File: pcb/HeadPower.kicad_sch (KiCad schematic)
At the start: 9 parts

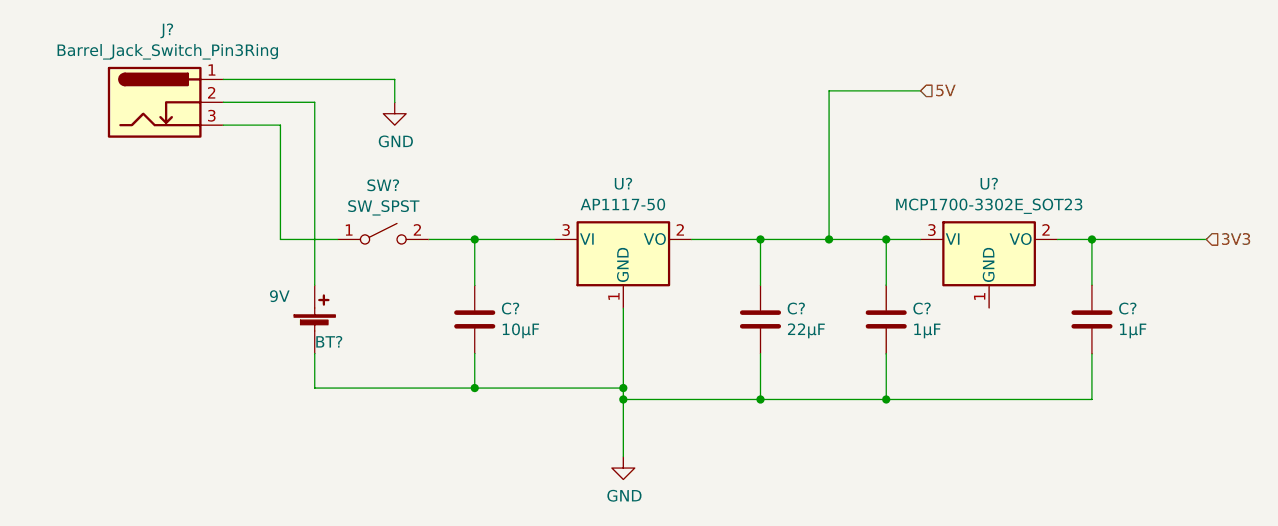
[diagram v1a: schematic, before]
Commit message: Adds line protection
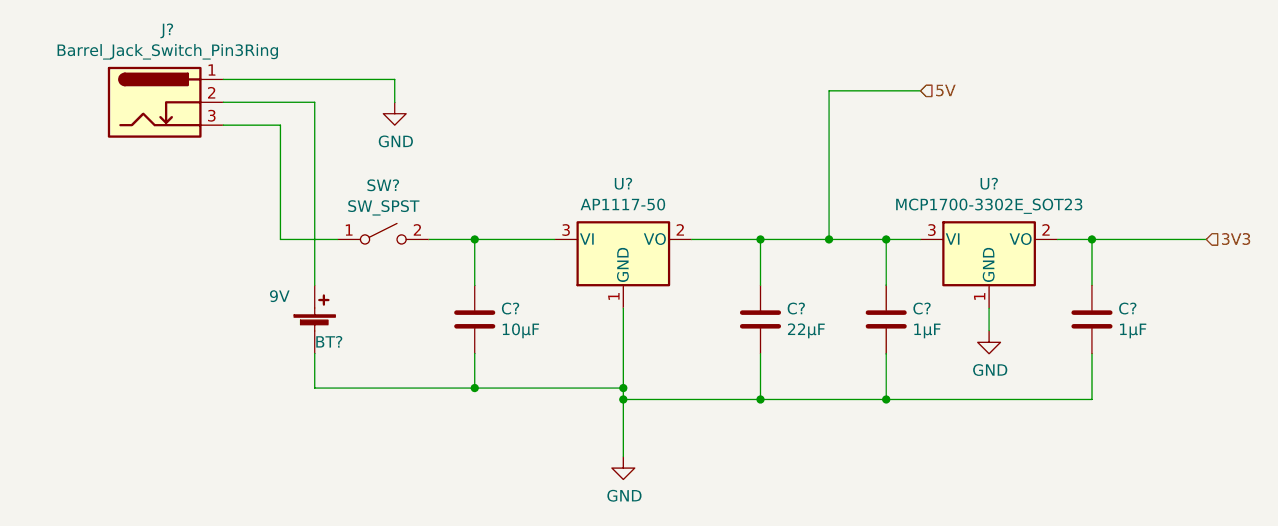
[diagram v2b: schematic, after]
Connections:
- net GND: now also U?.1 (GND)
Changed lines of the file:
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@@
+    (stroke (width 0) (type default) (color 0 0 0 0))
+  )
+  (wire (pts (xy 154.94 77.47) (xy 154.94 80.01))
     (stroke (width 0) (type default) (color 0 0 0 0))
   )
@@
     (pin "2")
   )
+  (symbol (lib_id "power:GND") (at 154.94 80.01 0) (unit 1)
+    (in_bom yes) (on_board yes)
+    (property "Reference" "#PWR?" (id 0) (at 154.94 86.36 0)
+      (effects (font (size 1.27 1.27)) hide)
+    )
+    (property "Value" "GND" (id 1) (at 155.067 84.4042 0))
+    (property "Footprint" "" (id 2) (at 154.94 80.01 0)
+      (effects (font (size 1.27 1.27)) hide)
+    )
+    (property "Datasheet" "" (id 3) (at 154.94 80.01 0)
+      (effects (font (size 1.27 1.27)) hide)
+    )
+    (pin "1")
+  )
 )

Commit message: Adds current control for the display adapter back light
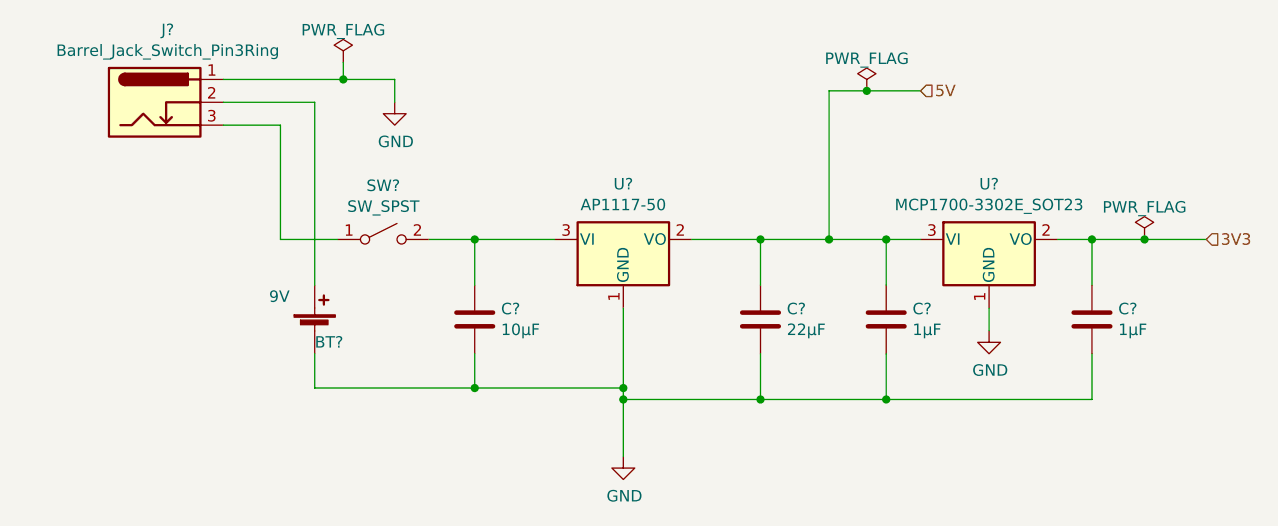
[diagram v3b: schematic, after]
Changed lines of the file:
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@@
   (junction (at 129.54 69.85) (diameter 0) (color 0 0 0 0)
   )
+  (junction (at 172.212 69.85) (diameter 0) (color 0 0 0 0)
+  )
   (junction (at 114.3 86.36) (diameter 0) (color 0 0 0 0)
   )
+  (junction (at 83.185 52.07) (diameter 0) (color 0 0 0 0)
+  )
   (junction (at 114.3 87.63) (diameter 0) (color 0 0 0 0)
   )
@@
   (junction (at 143.51 69.85) (diameter 0) (color 0 0 0 0)
   )
+  (junction (at 141.351 53.34) (diameter 0) (color 0 0 0 0)
+  )
   (wire (pts (xy 129.54 69.85) (xy 121.92 69.85))
     (stroke (width 0) (type default) (color 0 0 0 0))
@@
     (stroke (width 0) (type default) (color 0 0 0 0))
   )
-  (wire (pts (xy 166.37 69.85) (xy 179.07 69.85))
+  (wire (pts (xy 166.37 69.85) (xy 172.212 69.85))
     (stroke (width 0) (type default) (color 0 0 0 0))
   )
@@
     (stroke (width 0) (type default) (color 0 0 0 0))
   )
-  (wire (pts (xy 69.85 52.07) (xy 88.9 52.07))
-    (stroke (width 0) (type default) (color 0 0 0 0))
-  )
-  (wire (pts (xy 137.16 53.34) (xy 147.32 53.34))
+  (wire (pts (xy 69.85 52.07) (xy 83.185 52.07))
+    (stroke (width 0) (type default) (color 0 0 0 0))
+  )
+  (wire (pts (xy 137.16 53.34) (xy 141.351 53.34))
     (stroke (width 0) (type default) (color 0 0 0 0))
   )
@@
     (stroke (width 0) (type default) (color 0 0 0 0))
   )
+  (wire (pts (xy 141.351 53.34) (xy 147.32 53.34))
+    (stroke (width 0) (type default) (color 0 0 0 0))
+  )
   (wire (pts (xy 97.79 69.85) (xy 106.68 69.85))
     (stroke (width 0) (type default) (color 0 0 0 0))
@@
     (stroke (width 0) (type default) (color 0 0 0 0))
   )
+  (wire (pts (xy 83.185 50.165) (xy 83.185 52.07))
+    (stroke (width 0) (type default) (color 0 0 0 0))
+  )
+  (wire (pts (xy 172.212 69.85) (xy 179.07 69.85))
+    (stroke (width 0) (type default) (color 0 0 0 0))
+  )
   (wire (pts (xy 137.16 69.85) (xy 143.51 69.85))
     (stroke (width 0) (type default) (color 0 0 0 0))
@@
   )
   (wire (pts (xy 80.01 74.93) (xy 80.01 54.61))
+    (stroke (width 0) (type default) (color 0 0 0 0))
+  )
+  (wire (pts (xy 83.185 52.07) (xy 88.9 52.07))
     (stroke (width 0) (type default) (color 0 0 0 0))
   )
@@
     (pin "2")
   )
+  (symbol (lib_id "power:PWR_FLAG") (at 83.185 50.165 0) (unit 1)
+    (in_bom yes) (on_board yes) (fields_autoplaced)
+    (property "Reference" "#FLG?" (id 0) (at 83.185 48.26 0)
+      (effects (font (size 1.27 1.27)) hide)
+    )
+    (property "Value" "PWR_FLAG" (id 1) (at 83.185 46.5892 0))
+    (property "Footprint" "" (id 2) (at 83.185 50.165 0)
+      (effects (font (size 1.27 1.27)) hide)
+    )
+    (property "Datasheet" "~" (id 3) (at 83.185 50.165 0)
+      (effects (font (size 1.27 1.27)) hide)
+    )
+    (pin "1")
+  )
   (symbol (lib_id "power:GND") (at 154.94 80.01 0) (unit 1)
     (in_bom yes) (on_board yes)
@@
       (effects (font (size 1.27 1.27)) hide)
     )
+    (pin "1")
+  )
+  (symbol (lib_id "power:PWR_FLAG") (at 141.351 53.34 0) (unit 1)
+    (in_bom yes) (on_board yes) (fields_autoplaced)
+    (property "Reference" "#FLG?" (id 0) (at 141.351 51.435 0)
+      (effects (font (size 1.27 1.27)) hide)
+    )
+    (property "Value" "PWR_FLAG" (id 1) (at 141.351 49.7642 0))
+    (property "Footprint" "" (id 2) (at 141.351 53.34 0)
+      (effects (font (size 1.27 1.27)) hide)
+    )
+    (property "Datasheet" "~" (id 3) (at 141.351 53.34 0)
+      (effects (font (size 1.27 1.27)) hide)
+    )
+    (pin "1")
+  )
+  (symbol (lib_id "power:PWR_FLAG") (at 172.212 69.85 0) (unit 1)
+    (in_bom yes) (on_board yes) (fields_autoplaced)
+    (property "Reference" "#FLG?" (id 0) (at 172.212 67.945 0)
+      (effects (font (size 1.27 1.27)) hide)
+    )
+    (property "Value" "PWR_FLAG" (id 1) (at 172.212 66.2742 0))
+    (property "Footprint" "" (id 2) (at 172.212 69.85 0)
+      (effects (font (size 1.27 1.27)) hide)
+    )
+    (property "Datasheet" "~" (id 3) (at 172.212 69.85 0)
+      (effects (font (size 1.27 1.27)) hide)
+    )

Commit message: Schematic complete
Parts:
- gave numbers to parts that had none: 9
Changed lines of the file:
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@@
   (junction (at 129.54 69.85) (diameter 0) (color 0 0 0 0)
   )
-  (junction (at 172.212 69.85) (diameter 0) (color 0 0 0 0)
-  )
   (junction (at 114.3 86.36) (diameter 0) (color 0 0 0 0)
   )
@@
   (junction (at 166.37 69.85) (diameter 0) (color 0 0 0 0)
   )
+  (junction (at 103.378 69.85) (diameter 0) (color 0 0 0 0)
+  )
   (junction (at 137.16 69.85) (diameter 0) (color 0 0 0 0)
   )
@@
   (junction (at 143.51 69.85) (diameter 0) (color 0 0 0 0)
   )
-  (junction (at 141.351 53.34) (diameter 0) (color 0 0 0 0)
-  )
   (wire (pts (xy 129.54 69.85) (xy 121.92 69.85))
     (stroke (width 0) (type default) (color 0 0 0 0))
@@
     (stroke (width 0) (type default) (color 0 0 0 0))
   )
-  (wire (pts (xy 166.37 69.85) (xy 172.212 69.85))
+  (wire (pts (xy 166.37 69.85) (xy 179.07 69.85))
     (stroke (width 0) (type default) (color 0 0 0 0))
   )
@@
     (stroke (width 0) (type default) (color 0 0 0 0))
   )
+  (wire (pts (xy 103.378 69.85) (xy 106.68 69.85))
+    (stroke (width 0) (type default) (color 0 0 0 0))
+  )
   (wire (pts (xy 76.2 69.85) (xy 76.2 57.15))
     (stroke (width 0) (type default) (color 0 0 0 0))
@@
     (stroke (width 0) (type default) (color 0 0 0 0))
   )
-  (wire (pts (xy 137.16 53.34) (xy 141.351 53.34))
-    (stroke (width 0) (type default) (color 0 0 0 0))
-  )
   (wire (pts (xy 82.55 69.85) (xy 76.2 69.85))
     (stroke (width 0) (type default) (color 0 0 0 0))
@@
     (stroke (width 0) (type default) (color 0 0 0 0))
   )
-  (wire (pts (xy 141.351 53.34) (xy 147.32 53.34))
-    (stroke (width 0) (type default) (color 0 0 0 0))
-  )
-  (wire (pts (xy 97.79 69.85) (xy 106.68 69.85))
+  (wire (pts (xy 137.16 53.34) (xy 147.32 53.34))
+    (stroke (width 0) (type default) (color 0 0 0 0))
+  )
+  (wire (pts (xy 97.79 69.85) (xy 103.378 69.85))
     (stroke (width 0) (type default) (color 0 0 0 0))
   )
@@
   )
   (wire (pts (xy 83.185 50.165) (xy 83.185 52.07))
-    (stroke (width 0) (type default) (color 0 0 0 0))
-  )
-  (wire (pts (xy 172.212 69.85) (xy 179.07 69.85))
     (stroke (width 0) (type default) (color 0 0 0 0))
   )
@@
   (symbol (lib_id "Regulator_Linear:MCP1700-3302E_SOT23") (at 154.94 69.85 0) (unit 1)
     (in_bom yes) (on_board yes)
-    (property "Reference" "U?" (id 0) (at 154.94 63.7032 0))
+    (property "Reference" "U702" (id 0) (at 154.94 63.7032 0))
     (property "Value" "MCP1700-3302E_SOT23" (id 1) (at 154.94 66.0146 0))
     (property "Footprint" "Package_TO_SOT_SMD:SOT-23" (id 2) (at 154.94 64.135 0)
@@
   (symbol (lib_id "Regulator_Linear:AP1117-50") (at 114.3 69.85 0) (unit 1)
     (in_bom yes) (on_board yes)
-    (property "Reference" "U?" (id 0) (at 114.3 63.7032 0))
+    (property "Reference" "U701" (id 0) (at 114.3 63.7032 0))
     (property "Value" "AP1117-50" (id 1) (at 114.3 66.0146 0))
     (property "Footprint" "Package_TO_SOT_SMD:SOT-223-3_TabPin2" (id 2) (at 114.3 64.77 0)
@@
   (symbol (lib_id "Device:Battery_Cell") (at 80.01 80.01 0) (unit 1)
     (in_bom yes) (on_board yes)
-    (property "Reference" "BT?" (id 0) (at 80.01 81.28 0)
+    (property "Reference" "BT701" (id 0) (at 80.01 81.28 0)
       (effects (font (size 1.27 1.27)) (justify left))
     )
@@
   (symbol (lib_id "Device:C") (at 97.79 78.74 0) (unit 1)
     (in_bom yes) (on_board yes)
-    (property "Reference" "C?" (id 0) (at 100.711 77.5716 0)
+    (property "Reference" "C701" (id 0) (at 100.711 77.5716 0)
       (effects (font (size 1.27 1.27)) (justify left))
     )
@@
   (symbol (lib_id "Device:C") (at 129.54 78.74 0) (unit 1)
     (in_bom yes) (on_board yes)
-    (property "Reference" "C?" (id 0) (at 132.461 77.5716 0)
+    (property "Reference" "C702" (id 0) (at 132.461 77.5716 0)
       (effects (font (size 1.27 1.27)) (justify left))
     )
@@
   (symbol (lib_id "power:GND") (at 114.3 93.98 0) (unit 1)
     (in_bom yes) (on_board yes)
-    (property "Reference" "#PWR?" (id 0) (at 114.3 100.33 0)
+    (property "Reference" "#PWR0702" (id 0) (at 114.3 100.33 0)
       (effects (font (size 1.27 1.27)) hide)
     )
@@
   (symbol (lib_id "Device:C") (at 143.51 78.74 0) (unit 1)
     (in_bom yes) (on_board yes)
-    (property "Reference" "C?" (id 0) (at 146.431 77.5716 0)
+    (property "Reference" "C703" (id 0) (at 146.431 77.5716 0)
       (effects (font (size 1.27 1.27)) (justify left))
     )
@@
   (symbol (lib_id "Device:C") (at 166.37 78.74 0) (unit 1)
     (in_bom yes) (on_board yes)
-    (property "Reference" "C?" (id 0) (at 169.291 77.5716 0)
+    (property "Reference" "C704" (id 0) (at 169.291 77.5716 0)
       (effects (font (size 1.27 1.27)) (justify left))
     )
@@
   (symbol (lib_id "Connector:Barrel_Jack_Switch_Pin3Ring") (at 62.23 54.61 0) (unit 1)
     (in_bom yes) (on_board yes)
-    (property "Reference" "J?" (id 0) (at 63.6778 46.5582 0))
+    (property "Reference" "J701" (id 0) (at 63.6778 46.5582 0))
     (property "Value" "Barrel_Jack_Switch_Pin3Ring" (id 1) (at 63.6778 48.8696 0))
     (property "Footprint" "Connector_PinHeader_2.54mm:PinHeader_1x02_P2.54mm_Vertical" (id 2) (at 63.5 55.626 0)
@@
   (symbol (lib_id "power:GND") (at 88.9 54.61 0) (unit 1)
     (in_bom yes) (on_board yes)
-    (property "Reference" "#PWR?" (id 0) (at 88.9 60.96 0)
+    (property "Reference" "#PWR0701" (id 0) (at 88.9 60.96 0)
       (effects (font (size 1.27 1.27)) hide)
     )
@@
   (symbol (lib_id "Switch:SW_SPST") (at 87.63 69.85 0) (unit 1)
     (in_bom yes) (on_board yes)
-    (property "Reference" "SW?" (id 0) (at 87.63 63.881 0))
+    (property "Reference" "SW701" (id 0) (at 87.63 63.881 0))
     (property "Value" "SW_SPST" (id 1) (at 87.63 66.1924 0))
     (property "Footprint" "Connector_PinHeader_2.54mm:PinHeader_1x02_P2.54mm_Vertical" (id 2) (at 87.63 69.85 0)
@@
   (symbol (lib_id "power:PWR_FLAG") (at 83.185 50.165 0) (unit 1)
     (in_bom yes) (on_board yes) (fields_autoplaced)
-    (property "Reference" "#FLG?" (id 0) (at 83.185 48.26 0)
+    (property "Reference" "#FLG0701" (id 0) (at 83.185 48.26 0)
       (effects (font (size 1.27 1.27)) hide)
     )
@@
   (symbol (lib_id "power:GND") (at 154.94 80.01 0) (unit 1)
     (in_bom yes) (on_board yes)
-    (property "Reference" "#PWR?" (id 0) (at 154.94 86.36 0)
+    (property "Reference" "#PWR0703" (id 0) (at 154.94 86.36 0)
       (effects (font (size 1.27 1.27)) hide)
     )
@@
     (pin "1")
   )
-  (symbol (lib_id "power:PWR_FLAG") (at 141.351 53.34 0) (unit 1)
+  (symbol (lib_id "power:PWR_FLAG") (at 103.378 69.85 0) (unit 1)
     (in_bom yes) (on_board yes) (fields_autoplaced)
-    (property "Reference" "#FLG?" (id 0) (at 141.351 51.435 0)
-      (effects (font (size 1.27 1.27)) hide)
-    )
-    (property "Value" "PWR_FLAG" (id 1) (at 141.351 49.7642 0))
-    (property "Footprint" "" (id 2) (at 141.351 53.34 0)
-      (effects (font (size 1.27 1.27)) hide)
-    )
-    (property "Datasheet" "~" (id 3) (at 141.351 53.34 0)
-      (effects (font (size 1.27 1.27)) hide)
-    )
-    (pin "1")
-  )
-  (symbol (lib_id "power:PWR_FLAG") (at 172.212 69.85 0) (unit 1)
-    (in_bom yes) (on_board yes) (fields_autoplaced)
-    (property "Reference" "#FLG?" (id 0) (at 172.212 67.945 0)
-      (effects (font (size 1.27 1.27)) hide)
-    )
-    (property "Value" "PWR_FLAG" (id 1) (at 172.212 66.2742 0))
-    (property "Footprint" "" (id 2) (at 172.212 69.85 0)
-      (effects (font (size 1.27 1.27)) hide)
-    )
-    (property "Datasheet" "~" (id 3) (at 172.212 69.85 0)
-      (effects (font (size 1.27 1.27)) hide)
-    )
+    (property "Reference" "#FLG0702" (id 0) (at 103.378 67.945 0)
+      (effects (font (size 1.27 1.27)) hide)
+    )
+    (property "Value" "PWR_FLAG" (id 1) (at 103.378 66.2742 0))
+    (property "Footprint" "" (id 2) (at 103.378 69.85 0)
+      (effects (font (size 1.27 1.27)) hide)
+    )
+    (property "Datasheet" "~" (id 3) (at 103.378 69.85 0)
+      (effects (font (size 1.27 1.27)) hide)
+    )

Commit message: DRC pass
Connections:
- net 3V3 renamed Vdd
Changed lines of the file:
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@@
     (effects (font (size 1.27 1.27)) (justify left))
   )
-  (hierarchical_label "3V3" (shape input) (at 179.07 69.85 0)
+  (hierarchical_label "Vdd" (shape input) (at 179.07 69.85 0)
     (effects (font (size 1.27 1.27)) (justify left))
   )

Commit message: DRC OK
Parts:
- removed U702: MCP1700-3302E_SOT23, Package_TO_SOT_SMD:SOT-23, symbol Regulator_Linear:MCP1700-3302E_SOT23
- added U703: MCP1700x-330xxTT, Package_TO_SOT_SMD:SOT-23, symbol Regulator_Linear:MCP1700x-330xxTT
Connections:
- net 5V: now also U703.3 (VI)
- net GND: now also U703.1 (GND)
- net Vdd: now also U703.2 (VO)
